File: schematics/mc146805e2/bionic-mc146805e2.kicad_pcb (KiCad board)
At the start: 2 copper layers, 48.3 x 71.1 mm, 10 parts, among them J1 Bionic-P135, J2 Bionic-P245, U1 MC146805E2P, U2 74HCT126, U3 11AA010-I/TO

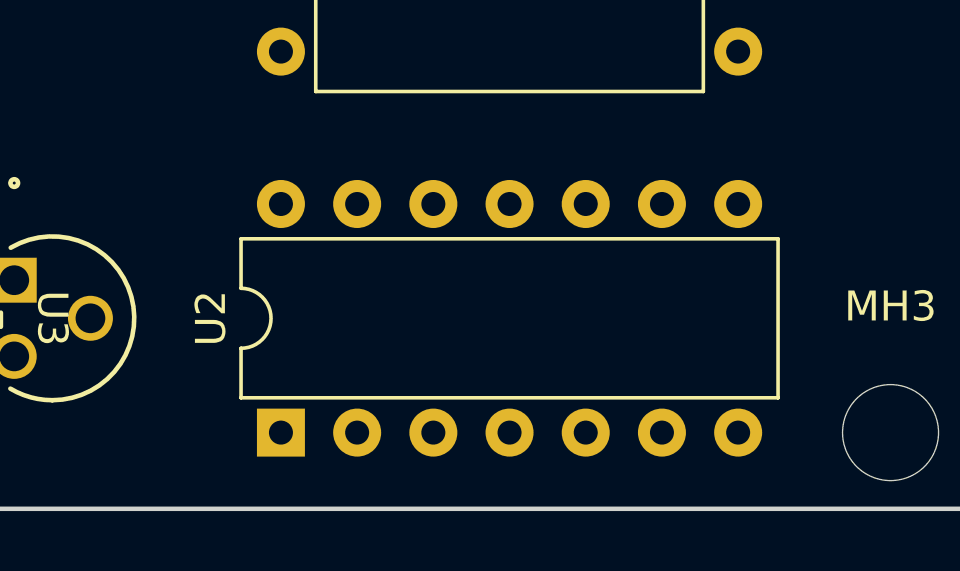
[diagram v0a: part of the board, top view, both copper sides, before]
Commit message: [MC146805E2] Remove HC126
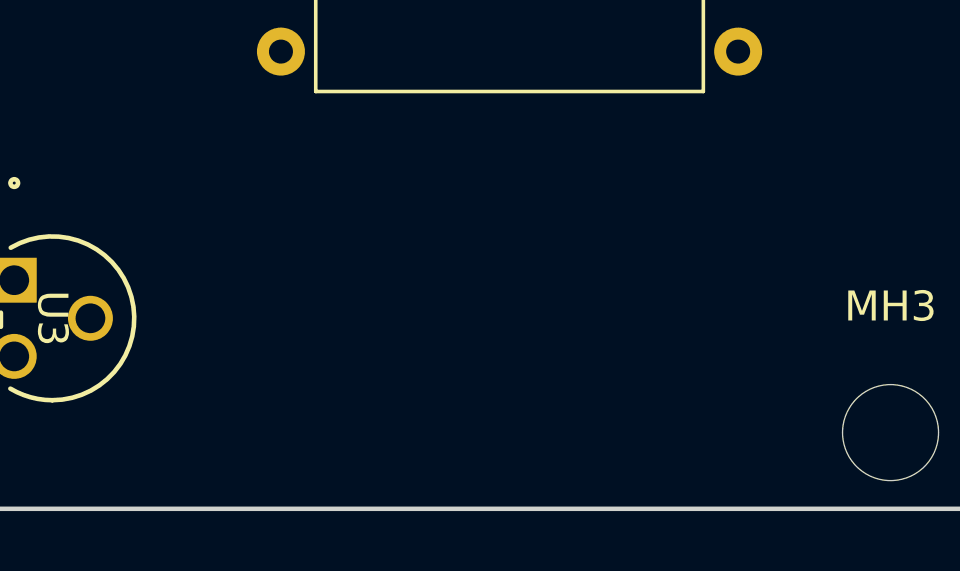
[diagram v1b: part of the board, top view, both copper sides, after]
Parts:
- removed U2: 74HCT126, Package_DIP:DIP-14_W7.62mm
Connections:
- U1 pad 1: Net-(U1-~{RESET}) -> /P53
- U1 pad 2: Net-(U1-~{IRQ}) -> /P42
- U1 pad 37: Net-(U1-TIMER) -> /P45
- U1 pad 39: Net-(U1-OSC1) -> /P46
